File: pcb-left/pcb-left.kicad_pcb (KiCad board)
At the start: 2 copper layers, 143.4 x 118.9 mm, 89 parts, among them J1 Conn_01x02_Pin, J2 Conn_01x06_MountingPin, J3 Conn_01x04_Pin, SW1 SW_Push, SW2 Rotary_Encoder_Default, U1 XC6206PxxxMR, U2 STM32F401RCTx, Y1 12MHz

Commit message: added new/renamed folders and files forgotten during last commits finished pcb-left
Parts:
- moved SW1 104.5 mm to (155.9, 52.8), turned to 90 degrees
- moved C10 94.0 mm to (157.0, 58.8), turned to 180 degrees
- moved J3 87.4 mm to (158.8, 43.7), turned to 90 degrees
- moved J1 65.8 mm to (176.8, 82.8)
- moved R7 30.0 mm to (157.9, 82.1), turned to -90 degrees
- moved R13 29.4 mm to (155.6, 82.1), turned to 90 degrees
- moved R8 16.5 mm to (163.3, 98.2)
- moved R10 12.9 mm to (163.3, 94.3), turned to 0 degrees
- moved R9 10.4 mm to (167.2, 98.2)
- moved R11 9.38 mm to (167.2, 94.3), turned to 0 degrees
- moved C9 4.95 mm to (162.4, 57.5), turned to 0 degrees
- moved C1 4.67 mm to (162.4, 55.4), turned to 0 degrees
- moved U1 3.05 mm to (162.5, 51.7)
- moved C8 2.70 mm to (165.7, 49.8)
- moved C4 2.25 mm to (173.8, 78.9), turned to -90 degrees
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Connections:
- U2 pad 50: /COL2 -> unconnected-(U2-PA15-Pad50)
- U2 pad 51: /COL3 -> unconnected-(U2-PC10-Pad51)
- U2 pad 52: /COL4 -> unconnected-(U2-PC11-Pad52)
- U2 pad 54: unconnected-(U2-PD2-Pad54) -> /COL4
- U2 pad 55: unconnected-(U2-PB3-Pad55) -> /COL3
- U2 pad 56: unconnected-(U2-PB4-Pad56) -> /COL2
- U2 pad 57: unconnected-(U2-PB5-Pad57) -> /COL1
- U2 pad 58: unconnected-(U2-PB6-Pad58) -> /COL0
- U2 pad 61: /COL0 -> unconnected-(U2-PB8-Pad61)
- U2 pad 62: /COL1 -> unconnected-(U2-PB9-Pad62)
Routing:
- net /COL0: track 57.2 -> 201.1 mm, vias 6 -> 10
- net /COL1: track 102.4 -> 225.2 mm, vias 8 -> 11
- net /COL2: track 108.4 -> 213.3 mm, vias 8 -> 11
- net /COL3: track 112.0 -> 196.8 mm, vias 8 -> 11
- net /COL4: track 121.3 -> 186.0 mm, vias 8 -> 11
- net /COL5: track 82.0 -> 128.9 mm, vias 6 -> 9
- net /SWCLK: track 0.00 -> 34.0 mm, vias 0 -> 1
- net /SWDIO: track 0.00 -> 32.3 mm, vias 0 -> 1
- net /nRESET: track 0.00 -> 30.9 mm, vias 0 -> 1
- net /ENC_A: track 0.00 -> 23.7 mm
- net /ENC_B: track 0.00 -> 19.7 mm
- net /HANDEDNESS: track 0.00 -> 13.3 mm
- net /BOOTSEL: track 0.00 -> 13.2 mm
- net /SPLIT_RX: track 0.00 -> 11.3 mm
- net /SPLIT_TX: track 0.00 -> 11.0 mm, vias 0 -> 2
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
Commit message: quick save
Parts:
- removed R10, R8: 5.1k, Resistor_SMD:R_0603_1608Metric
- removed R12: 1k, Resistor_SMD:R_0603_1608Metric
- added C14: 100n, Capacitor_SMD:C_0603_1608Metric, B.Cu at (158.6, 43.2)
- added D30: ~, lib-zegonix:SK6812MINI-E_3.2x2.8_reverse_mount, F.Cu at (165.3, 43.2)
- C10, R3, R5, SW1: moved to B.Cu
- C12, C13: value 22p -> 12p
- J2: footprint Connector_JST:JST_SHL_SM06B-SHLS-TF_1x06-1MP_P1.00mm_Horizontal -> Connector_JST:JST_SH_SM06B-SRSS-TB_1x06-1MP_P1.00mm_Horizontal; moved to B.Cu
- R1, R2: value 27 -> 10k; moved to B.Cu
- R11, R13, R7, R9: value 5.1k -> 10k
- Y1: value 12MHz -> 8MHz
- moved SW1 59.5 mm to (170.3, 110.5)
- moved C10 47.0 mm to (169.2, 104.2), turned to 0 degrees
- moved R1 30.3 mm to (176.3, 90.0), turned to 180 degrees
- moved R2 15.5 mm to (153.4, 66.4), turned to 90 degrees
- moved C8 8.70 mm to (157.0, 49.7), turned to 0 degrees
- moved J3 7.45 mm to (160.7, 36.5)
- moved C1 6.43 mm to (156.1, 56.7)
- moved U1 6.43 mm to (156.2, 53.0)
- moved C9 6.43 mm to (156.1, 58.8)
- moved J1 4.48 mm to (174.6, 86.7), turned to 90 degrees
- moved J2 3.91 mm to (174.3, 54.0)
- moved R3 2.71 mm to (164.8, 59.6)
- moved R5 2.70 mm to (162.6, 59.6)
- moved C12 1.04 mm to (172.2, 82.9)
- moved C13 1.04 mm to (168.8, 86.7)
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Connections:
- C13 pad 2: Net-(C13-Pad2) -> /XOUT
- J1 pad 1: /BOOTSEL -> +3V3
- J1 pad 2: GND -> /BOOT0
- R1 pad 1: /USB_D- -> /BOOT0
- R1 pad 2: Net-(U2-PA11) -> GND
- R11 pad 1: Net-(R10-Pad2) -> /ENC_B
- R2 pad 1: /USB_D+ -> /BOOT1
- R2 pad 2: Net-(U2-PA12) -> GND
- R9 pad 2: Net-(R8-Pad1) -> /ENC_A
- U2 pad 28: unconnected-(U2-PB2-Pad28) -> /BOOT1
- U2 pad 34: unconnected-(U2-PB13-Pad34) -> /IND_LED
- U2 pad 44: Net-(U2-PA11) -> /USB_D-
- U2 pad 45: Net-(U2-PA12) -> /USB_D+
- U2 pad 60: /BOOTSEL -> /BOOT0
- Y1 pad 1: Net-(C13-Pad2) -> /XOUT
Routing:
- net /IND_LED: track 0.00 -> 32.7 mm, vias 0 -> 2
- net +3V3: track 111.0 -> 138.9 mm, vias 3 -> 4
- net /BOOT0: track 0.00 -> 20.4 mm
- net +5V: track 15.2 -> 33.3 mm, vias 1 -> 0
- net /BOOTSEL: track 13.2 -> 0.00 mm
- net /SWCLK: track 34.0 -> 45.8 mm, vias 1 -> 0
- net /USB_D-: track 8.88 -> 17.6 mm
- net /USB_D+: track 7.97 -> 16.5 mm
- net /BOOT1: track 0.00 -> 7.17 mm
- net /nRESET: track 30.9 -> 37.5 mm, vias 1 -> 2
- net GND: track 24.3 -> 30.4 mm, vias 34 -> 239
- net /SPLIT_RX: track 11.3 -> 16.5 mm
- net Net-(C13-Pad2): track 5.10 -> 0.00 mm
- net /XOUT: track 5.76 -> 10.2 mm
- net Net-(U2-PA12): track 4.17 -> 0.00 mm, vias 1 -> 0
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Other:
- outline, holes or cut-outs redrawn

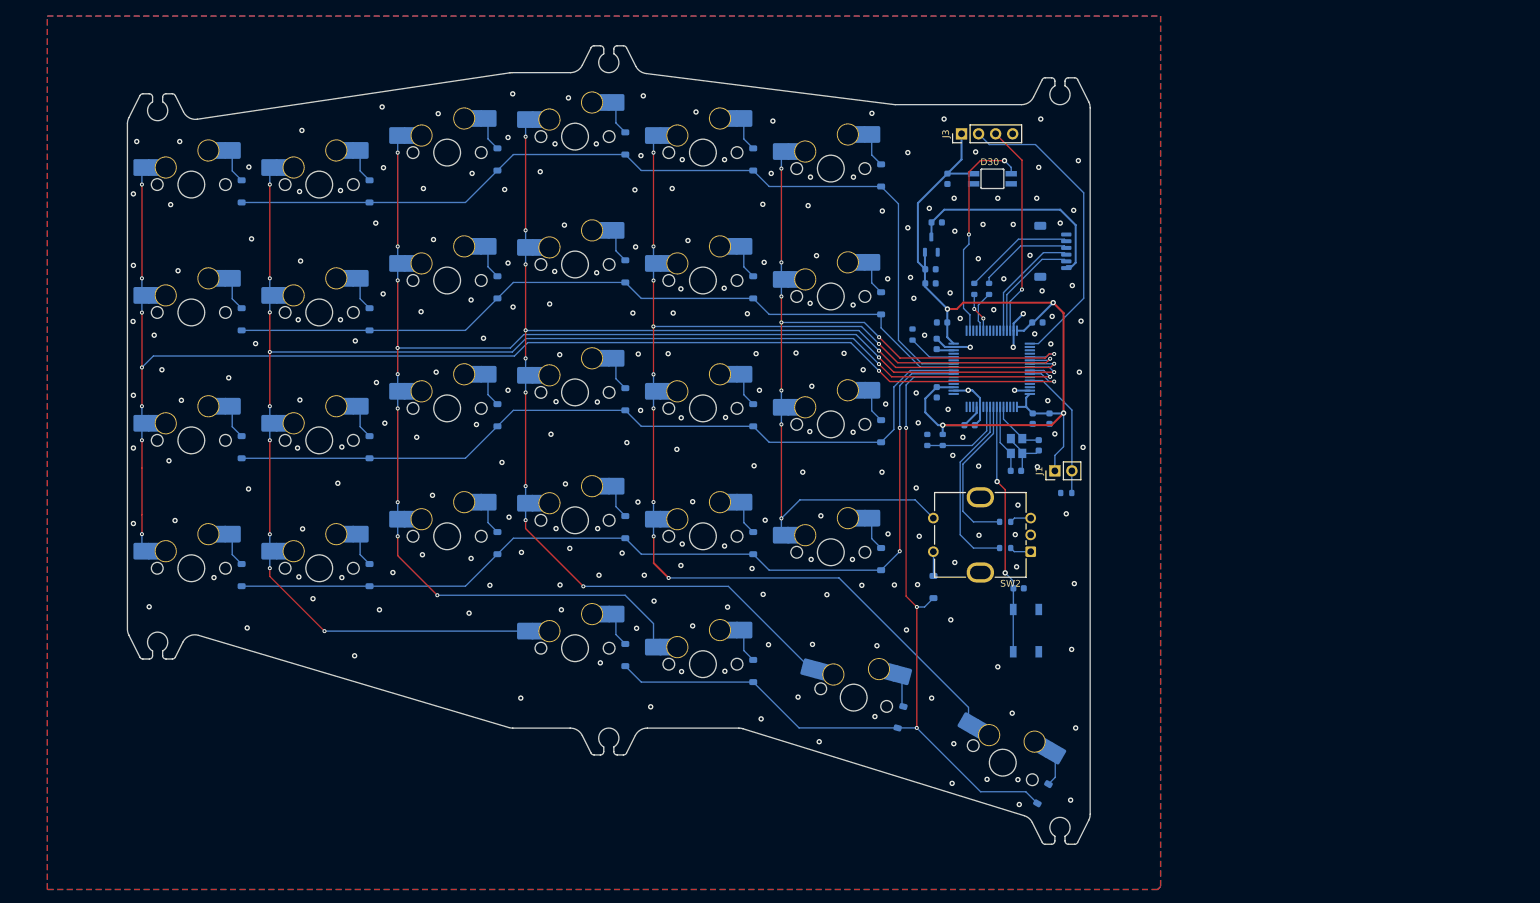
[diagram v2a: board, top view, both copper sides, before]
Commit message: finalised first version of pcbs for prototype order added openscad file for the left halfs case
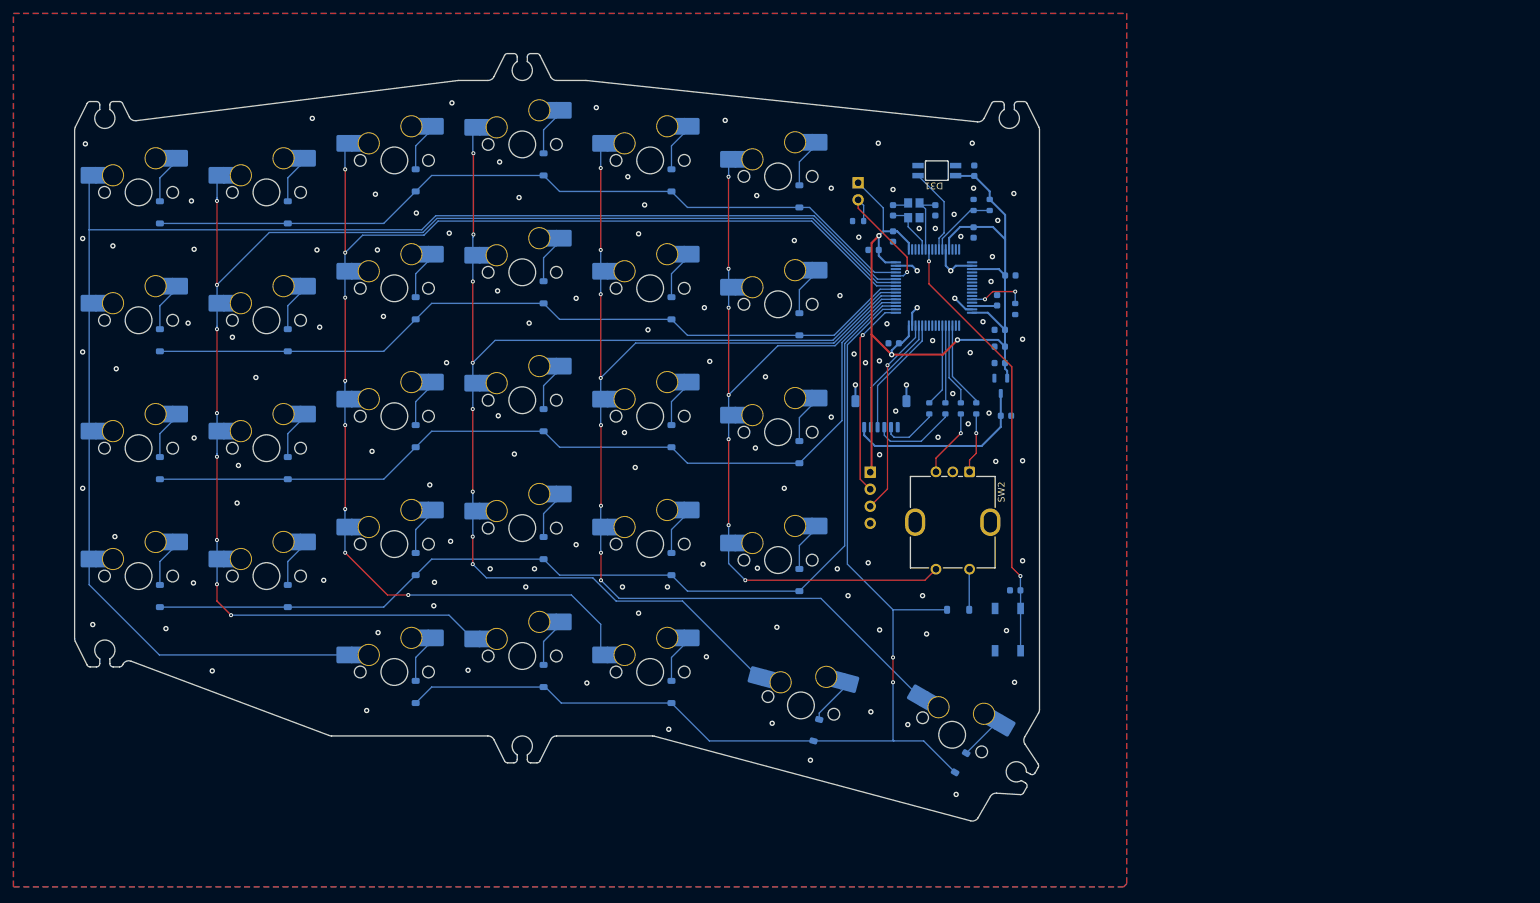
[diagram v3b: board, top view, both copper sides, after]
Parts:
- removed R11, R13: 10k, Resistor_SMD:R_0603_1608Metric
- added D31: ~, lib-zegonix:SK6812MINI-E_3.2x2.8_reverse_mount, F.Cu at (157.0, 42.0)
- added MX29: MX_SW_HS, PCM_marbastlib-mx:SW_MX_HS_1u, B.Cu at (159.3, 126.0)
- added R10: 10k, Resistor_SMD:R_0603_1608Metric, B.Cu at (162.5, 47.1)
- added R8: 10k, Resistor_SMD:R_0603_1608Metric, B.Cu at (162.9, 77.4)
- C10: value 100n -> 1u
- C13: value 12p -> 100n
- C14: value 100n -> 12p
- C8: value 1u -> 100n
- D30: value ~ -> D_Small; footprint lib-zegonix:SK6812MINI-E_3.2x2.8_reverse_mount -> Diode_SMD:D_SOD-123; moved to B.Cu
- J1: moved to B.Cu
- J2: value Conn_01x06_MountingPin -> Conn_01x04_Pin; footprint Connector_JST:JST_SH_SM06B-SRSS-TB_1x06-1MP_P1.00mm_Horizontal -> Connector_PinHeader_2.54mm:PinHeader_1x04_P2.54mm_Vertical
- J3: value Conn_01x04_Pin -> Conn_01x06_MountingPin; footprint Connector_PinHeader_2.54mm:PinHeader_1x04_P2.54mm_Vertical -> Connector_JST:JST_SH_SM06B-SRSS-TB_1x06-1MP_P1.00mm_Horizontal; moved to B.Cu
- moved D30 64.4 mm to (160.2, 107.4)
- moved C8 56.0 mm to (168.7, 104.5), turned to 180 degrees
- moved J1 52.0 mm to (145.3, 43.8), turned to 180 degrees
- moved R1 51.0 mm to (145.3, 49.5)
- moved C13 45.1 mm to (162.6, 42.0), turned to 90 degrees
- moved J3 43.4 mm to (148.7, 78.2), turned to 0 degrees
- moved J2 42.7 mm to (147.1, 86.9), turned to 180 degrees
- moved C12 41.2 mm to (150.5, 47.9), turned to -90 degrees
- moved Y1 38.3 mm to (153.6, 47.9), turned to -90 degrees
- moved C4 35.8 mm to (150.5, 51.8)
- moved R7 35.7 mm to (164.9, 47.1)
- moved D28 35.0 mm to (139.1, 125.4), turned to 75 degrees
- moved D27 34.3 mm to (117.5, 119.7), turned to 90 degrees
- moved C10 33.7 mm to (166.4, 70.7), turned to 180 degrees
- moved D25 31.7 mm to (79.4, 119.7)
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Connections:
- C10 pad 1: /nRESET -> +3V3
- C13 pad 1: GND -> +3V3
- C13 pad 2: /XOUT -> GND
- C14 pad 1: +3V3 -> GND
- C14 pad 2: GND -> /XOUT
- C8 pad 1: +5V -> /nRESET
- C9 pad 1: +3V3 -> +5V
- D29 pad 2: /ENC_SW_2 -> Net-(D29-A)
- D30 pad 1: +3V3 -> /ROW4
- D30 pad 2: unconnected-(D30-DOUT-Pad2) -> /ENC_SW_2
- J2 pad 1: +5V -> +3V3
- J2 pad 2: /USB_D+ -> /SWCLK
- J2 pad 3: /USB_D- -> /SWDIO
- J2 pad 4: /SPLIT_TX -> GND
- J3 pad 1: +3V3 -> +5V
- J3 pad 2: /SWCLK -> /USB_D+
- J3 pad 3: /SWDIO -> /USB_D-
- J3 pad 4: GND -> /SPLIT_TX
- MX25 pad 1: /COL1 -> /COL0
- MX26 pad 1: /COL2 -> /COL1
- MX27 pad 1: /COL3 -> /COL2
- MX28 pad 1: /COL4 -> /COL3
- R9 pad 1: Net-(R9-Pad1) -> /ENC_B
- R9 pad 2: /ENC_A -> Net-(R9-Pad2)
- SW2 pad A: Net-(R9-Pad1) -> Net-(R8-Pad1)
- SW2 pad B: Net-(R11-Pad2) -> Net-(R9-Pad2)
- U2 pad 10: /HANDEDNESS -> /IND_LED
- U2 pad 11: unconnected-(U2-PC3-Pad11) -> /HANDEDNESS
- U2 pad 22: /ROW4 -> unconnected-(U2-PA6-Pad22)
- U2 pad 23: /ROW3 -> unconnected-(U2-PA7-Pad23)
- U2 pad 24: /ROW2 -> unconnected-(U2-PC4-Pad24)
- U2 pad 25: /ROW1 -> unconnected-(U2-PC5-Pad25)
- U2 pad 26: /ROW0 -> unconnected-(U2-PB0-Pad26)
- U2 pad 34: /IND_LED -> unconnected-(U2-PB13-Pad34)
- U2 pad 35: unconnected-(U2-PB14-Pad35) -> /ENC_A
- U2 pad 36: unconnected-(U2-PB15-Pad36) -> /ENC_B
- U2 pad 50: unconnected-(U2-PA15-Pad50) -> /ROW4
- U2 pad 51: unconnected-(U2-PC10-Pad51) -> /ROW3
- U2 pad 52: unconnected-(U2-PC11-Pad52) -> /ROW2
- U2 pad 56: /COL2 -> /ROW1
- U2 pad 57: /COL1 -> /COL2
- U2 pad 58: /COL0 -> /COL1
- U2 pad 59: unconnected-(U2-PB7-Pad59) -> /COL0
- U2 pad 61: unconnected-(U2-PB8-Pad61) -> /ROW0
- U2 pad 8: /ENC_B -> unconnected-(U2-PC0-Pad8)
- U2 pad 9: /ENC_A -> unconnected-(U2-PC1-Pad9)
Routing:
- net /ROW4: track 132.2 -> 165.9 mm, vias 3 -> 2
- net /nRESET: track 37.5 -> 65.7 mm
- net /COL0: track 201.1 -> 228.4 mm, vias 9 -> 0
- net /IND_LED: track 32.7 -> 12.9 mm, vias 2 -> 0
- net /COL4: track 186.6 -> 168.4 mm, vias 11 -> 8
- net /COL2: track 213.3 -> 196.1 mm, vias 11 -> 8
- net /SWCLK: track 45.8 -> 30.1 mm, vias 0 -> 1
- net /ROW0: track 133.8 -> 118.6 mm
- net /COL3: track 196.8 -> 181.9 mm, vias 11 -> 8
- net /ENC_A: track 27.6 -> 13.0 mm
- net /ROW3: track 137.6 -> 149.8 mm, vias 2 -> 0
- net /ROW2: track 119.1 -> 131.3 mm
- net /COL1: track 225.2 -> 213.1 mm, vias 11 -> 8
- net /ENC_B: track 23.6 -> 12.2 mm
- net Net-(R9-Pad2): track 0.00 -> 10.2 mm, vias 0 -> 1
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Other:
- board size 143.4 x 118.9 mm -> 143.7 x 114.3 mm
